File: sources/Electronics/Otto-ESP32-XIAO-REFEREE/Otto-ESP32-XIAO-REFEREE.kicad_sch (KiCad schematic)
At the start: 22 parts, among them J1 Industrial Sensor, J12 OLED 0,91" - I2C (SKU21796), J7 Ultrasonic sensor, J8 Barrel_Jack_Switch, SW1 SW_SPDT, SW4 CherryMX, SW5 CherryMX, SW6 CherryMX, U1 MOUDLE-SEEEDUINO-XIAO-ESP32C3, U2 R-78E5.0-1.0

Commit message: update Schematics
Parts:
- added J2: Industrial Sensor, Connector_Molex:Molex_KK-254_AE-6410-04A_1x04_P2.54mm_Vertical, symbol Connector_Generic:Conn_01x04
- added R2, R3: 10K, Resistor_SMD:R_1206_3216Metric_Pad1.30x1.75mm_HandSolder, symbol Device:R_Small
- added R4: 220, Resistor_SMD:R_1206_3216Metric_Pad1.30x1.75mm_HandSolder, symbol Device:R_Small
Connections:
- net SENSOR_NPN is gone; now on net SENSOR_NPN_1: J1.3 (Pin_3)
- net +12V: now also J2.2 (Pin_2)
- net +3.3V: now also R2.1, R3.1
- net GND: now also J2.1 (Pin_1)
- net Key01: now also U1.10 (PA5_A9_D9_MISO)
- net Key02: now also U1.9 (PA7_A8_D8_SCK)
- net Key03: now also U1.8 (PB09_A7_D7_RX)
- net LED: now also R4.1
- net SENSOR_NPN_2: now reaches U1.11 (PA6_A10_D10_MOSI)
- net SENSOR_NPN_2: now also J2.3 (Pin_3), R3.2
- net SENSOR_NPN_1: now reaches U1.4 (PA11_A3_D3)
- net SENSOR_NPN_1: now also R2.2
- net at U1.7 (PB08_A6_D6_TX): now also R4.2
- net SENSOR_PNP: no longer names the net of J1.4 (Pin_4)
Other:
- moved on the sheet: BZ1, D4, J1, J12, J7, SW4, SW5, SW6, U1

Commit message: add silkscreen
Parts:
- removed R4: 220, Resistor_SMD:R_1206_3216Metric_Pad1.30x1.75mm_HandSolder, symbol Device:R_Small
- added R5: 330, Resistor_SMD:R_1206_3216Metric_Pad1.30x1.75mm_HandSolder, symbol Device:R_Small
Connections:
- net +3.3V: no longer C5.2, C6.2, C7.2, D2.1 (VDD), D3.1 (VDD), D5.1 (VDD)
- net +5V: now also C5.2, C6.2, C7.2, D2.1 (VDD), D3.1 (VDD), D5.1 (VDD)
- net LED: now also U1.7 (PB08_A6_D6_TX), R5.1; no longer D2.4 (DIN)
- new net: D2.4 (DIN), R5.2
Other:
- moved on the sheet: D2, D3, D5

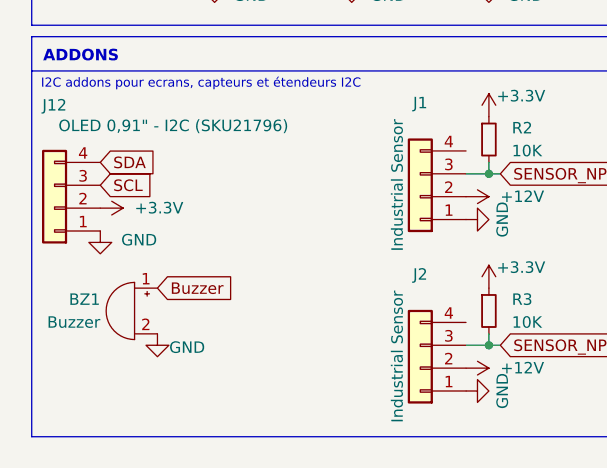
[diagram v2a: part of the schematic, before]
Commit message: add I2C resistors
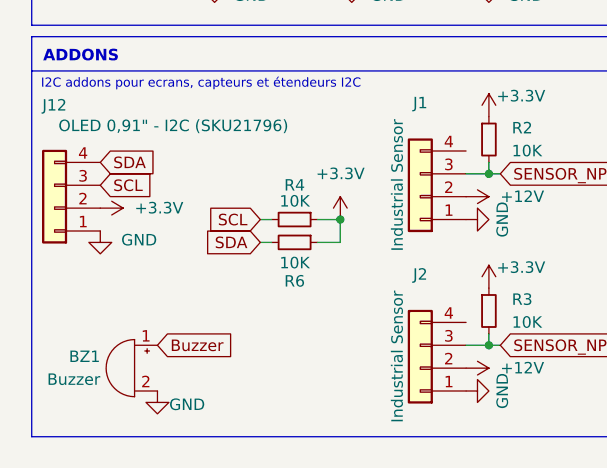
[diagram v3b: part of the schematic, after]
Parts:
- added R4, R6: 10K, Resistor_SMD:R_1206_3216Metric_Pad1.30x1.75mm_HandSolder, symbol Device:R_Small
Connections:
- net +3.3V: now also R4.1, R6.1
- net SCL: now also R4.2
- net SDA: now also R6.2
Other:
- moved on the sheet: BZ1
